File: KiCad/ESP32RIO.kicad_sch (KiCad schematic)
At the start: 44 parts, among them J1 Screw_Terminal_01x08, J2 Screw_Terminal_01x08, J3 Screw_Terminal_01x08, J4 Screw_Terminal_01x08, Q1 BC548, Q2 BC548, U1 PC817, U10 PC817, U11 PC817, U12 PC817, U13 PC817, U14 PC817, U15 LM7812_TO220, U16 ESP32-DEVKIT-V1, U17 XTR115U, U18 XTR115U, U19 PCF8574, U2 PC817, U20 ULN2803A, U21 TB67H451FNG, U22 SP3485CN, U3 PC817, U4 PC817, U5 PC817, U6 PC817, U7 PC817, U8 PC817, U9 PC817

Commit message: Versjon1
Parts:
- removed J1, J2, J3, J4: Screw_Terminal_01x08, TerminalBlock_Phoenix:TerminalBlock_Phoenix_MKDS-1,5-8-5.08_1x08_P5.08mm_Horizontal, symbol Connector:Screw_Terminal_01x08
- removed Q1, Q2: BC548, Package_TO_SOT_THT:TO-92_Inline, symbol Transistor_BJT:BC548
- removed U11, U12, U13, U14: PC817, Package_DIP:DIP-4_W7.62mm, symbol Isolator:PC817
- removed U15: LM7812_TO220, Package_TO_SOT_THT:TO-220-3_Vertical, symbol Regulator_Linear:LM7812_TO220
- removed U16: ESP32-DEVKIT-V1, doit-esp32-devkit-kicad:ESP32-DOIT-DEVKIT, symbol Devkit V1-1:ESP32-DEVKIT-V1
- removed U17, U18: XTR115U, Package_SO:SOIC-8_3.9x4.9mm_P1.27mm, symbol Interface_CurrentLoop:XTR115U
- removed U19: PCF8574, Package_DIP:DIP-18_W7.62mm, symbol Interface_Expansion:PCF8574
- removed U20: ULN2803A, Package_DIP:DIP-18_W7.62mm, symbol Transistor_Array:ULN2803A
- added C2, C3: 0.1uF, Capacitor_SMD:C_1206_3216Metric_Pad1.33x1.80mm_HandSolder, symbol RS485_Breakout-eagle-import:0.1UF-25V(+80/-20%)(0603)
- added C4: 47uF, Capacitor_THT:CP_Radial_D4.0mm_P2.00mm, symbol RS485_Breakout-eagle-import:0.1UF-25V(+80/-20%)(0603)
- added J1, J2: Screw_Terminal_01x12, TerminalBlock_Phoenix:TerminalBlock_Phoenix_MKDS-1,5-12_1x12_P5.00mm_Horizontal, symbol Connector:Screw_Terminal_01x12
- added R16, R17: R, Resistor_THT:R_Axial_DIN0204_L3.6mm_D1.6mm_P2.54mm_Vertical, symbol Device:R
- added U11: WeMos_S2_mini, wemos 2s mini:WEMOS_S2_mini, symbol Wemos s2 mini:WeMos_S2_mini
- added U12, U13, U14, U16: TLP222A, Package_DIP:DIP-4_W7.62mm, symbol Relay_SolidState:TLP222A
- added U15: L7805, Package_TO_SOT_SMD:TO-263-2, symbol Regulator_Linear:L7805
- C1: footprint RS485_Breakout:0603-CAP -> Capacitor_SMD:C_1206_3216Metric_Pad1.33x1.80mm_HandSolder
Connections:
- net +24V: now also J1.3 (Pin_3), U15.1 (IN)
- net GND: now also C1.2, U1.3, U10.3, U2.3, U21.1 (GND), U21.7 (RS), U21.9 (PAD), U22.5 (GND), U3.3, U4.3, U5.3, U6.3, U7.3, U8.3, U9.3, C2.1, C3.2, C4.1, J1.9 (Pin_9), R16.1, R17.1, U11.10 (GND), U11.26 (GND), U12.2, U13.2, U14.2, U15.2 (GND), U16.2
- net RTS: now also U11.23 (GPIO13)
- net RX-I: now also U11.7 (GPIO12)
- net TX-O: now also U11.24 (GPIO14)
- net at R4.2: now also J2.4 (Pin_4)
- net at R6.2: now also J2.6 (Pin_6)
- net at R15.1, U22.6 (A): now also J1.1 (Pin_1)
- net at R15.2, U22.7 (B): now also J1.2 (Pin_2)
- net at U10.4: now also U11.12 (GPIO18)
- net at R7.2: now also J2.7 (Pin_7)
- net at U6.4: now also U11.14 (GPIO35)
- net at U3.4: now also U11.31 (GPIO38)
- net at R13.1: now also U14.1
- net at C1.1: now also U21.4 (VREF), U22.8 (VCC), C3.1, U11.8 (3V3)
- net at R2.2: now also J2.2 (Pin_2)
- net at R13.2: now also U11.22 (GPIO10)
- net at R14.1: now also U16.1
- net at R14.2: now also U11.6 (GPIO11)
- net at R9.2: now also J2.9 (Pin_9)
- net at U7.4: now also U11.29 (GPIO34)
- net at U21.5 (VM): now also C2.2, C4.2, J1.10 (Pin_10)
- net at U21.8 (OUT2): now also J1.12 (Pin_12)
- net at U21.6 (OUT1): now also J1.11 (Pin_11)
- net at R12.1: now also U13.1
- net at R8.2: now also J2.8 (Pin_8)
- net at U4.4: now also U11.15 (GPIO37)
- net at R12.2: now also U11.5 (GPIO9)
- net at U1.4: now also U11.32 (GPIO40)
- net at R10.2: now also J2.10 (Pin_10)
- net at R11.1: now also U12.1
- net at R5.2: now also J2.5 (Pin_5)
- net at U2.4: now also U11.16 (GPIO39)
- net at U21.2 (IN2): now also U11.18 (GPIO2)
- net at U21.3 (IN1): now also U11.2 (GPIO3)
- net at R1.2: now also J2.1 (Pin_1)
- net at U9.4: now also U11.28 (GPIO21)
- net at R3.2: now also J2.3 (Pin_3)
- net at U8.4: now also U11.13 (GPIO33)
- net at R11.2: now also U11.21 (GPIO8)
- net at U5.4: now also U11.30 (GPIO36)
- new net: J2.12 (Pin_12), R16.2, U11.27 (GPIO17)
- new net: J2.11 (Pin_11), R17.2, U11.11 (GPIO16)
- new net: U11.9 (VBUS), U15.3 (OUT)
- new net: J1.4 (Pin_4), U12.3, U13.3, U14.3, U16.3
- new net: J1.5 (Pin_5), U16.4
- new net: J1.6 (Pin_6), U14.4
- new net: J1.7 (Pin_7), U13.4
- new net: J1.8 (Pin_8), U12.4
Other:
- note removed: "AI1"
- note removed: "AI2"
- note removed: "D2 må ha egen pullup motstand"
- note removed: "DAC"
- note removed: "Må bruke AM 422-1"
- moved on the sheet: C1, U21

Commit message: v1 sendt til produksjon
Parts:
- R11: value R -> 120R
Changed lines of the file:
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@@
       (effects (font (size 1.27 1.27)))
     )
-    (property "Value" "R" (at 220.98 55.4736 90)
+    (property "Value" "120R" (at 220.98 55.4736 90)
       (effects (font (size 1.27 1.27)))
     )

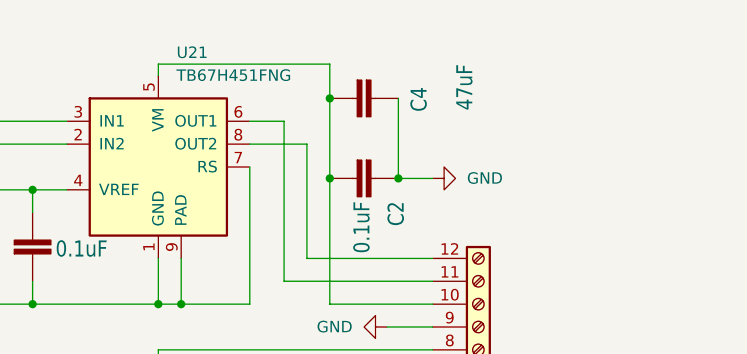
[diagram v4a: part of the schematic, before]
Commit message: fix kondensator og regulator
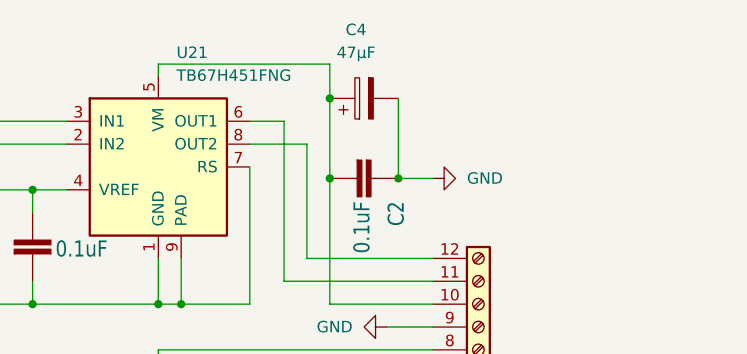
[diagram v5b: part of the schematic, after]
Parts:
- removed C4: 47uF, Capacitor_THT:CP_Radial_D4.0mm_P2.00mm, symbol RS485_Breakout-eagle-import:0.1UF-25V(+80/-20%)(0603)
- added C4: 47µF, Capacitor_THT:CP_Radial_D5.0mm_P2.50mm, symbol Device:C_Polarized
- U15: footprint Package_TO_SOT_SMD:TO-263-2 -> Package_TO_SOT_SMD:TO-252-2
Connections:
- net GND: now also C4.2
- net at C2.2, J1.10 (Pin_10), U21.5 (VM): now also C4.1
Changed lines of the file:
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@@
   (junction (at 229.87 163.83) (diameter 0) (color 0 0 0 0)
   )
+  (junction (at 64.77 72.39) (diameter 0) (color 0 0 0 0)
+  )
+  (junction (at 275.59 91.44) (diameter 0) (color 0 0 0 0)
+  )
+  (junction (at 85.09 132.08) (diameter 0) (color 0 0 0 0)
+  )
+  (junction (at 64.77 99.06) (diameter 0) (color 0 0 0 0)
+  )
+  (junction (at 85.09 116.84) (diameter 0) (color 0 0 0 0)
+  )
+  (junction (at 85.09 72.39) (diameter 0) (color 0 0 0 0)
+  )
+  (junction (at 64.77 107.95) (diameter 0) (color 0 0 0 0)
+  )
+  (junction (at 85.09 125.73) (diameter 0) (color 0 0 0 0)
+  )
+  (junction (at 255.27 95.25) (diameter 0) (color 0 0 0 0)
+  )
+  (junction (at 255.27 63.5) (diameter 0) (color 0 0 0 0)
+  )
+  (junction (at 45.72 90.17) (diameter 0) (color 0 0 0 0)
+  )
+  (junction (at 64.77 54.61) (diameter 0) (color 0 0 0 0)
+  )
+  (junction (at 85.09 90.17) (diameter 0) (color 0 0 0 0)
+  )
+  (junction (at 151.13 132.08) (diameter 0) (color 0 0 0 0)
+  )
+  (junction (at 247.65 40.64) (diameter 0) (color 0 0 0 0)
+  )
+  (junction (at 125.73 132.08) (diameter 0) (color 0 0 0 0)
+  )
   (junction (at 264.16 17.78) (diameter 0) (color 0 0 0 0)
   )
-  (junction (at 64.77 72.39) (diameter 0) (color 0 0 0 0)
-  )
-  (junction (at 275.59 91.44) (diameter 0) (color 0 0 0 0)
-  )
-  (junction (at 85.09 132.08) (diameter 0) (color 0 0 0 0)
-  )
-  (junction (at 64.77 99.06) (diameter 0) (color 0 0 0 0)
-  )
-  (junction (at 85.09 116.84) (diameter 0) (color 0 0 0 0)
-  )
-  (junction (at 85.09 72.39) (diameter 0) (color 0 0 0 0)
-  )
-  (junction (at 64.77 107.95) (diameter 0) (color 0 0 0 0)
-  )
-  (junction (at 85.09 125.73) (diameter 0) (color 0 0 0 0)
-  )
-  (junction (at 255.27 95.25) (diameter 0) (color 0 0 0 0)
-  )
-  (junction (at 255.27 63.5) (diameter 0) (color 0 0 0 0)
-  )
-  (junction (at 45.72 90.17) (diameter 0) (color 0 0 0 0)
-  )
-  (junction (at 64.77 54.61) (diameter 0) (color 0 0 0 0)
-  )
-  (junction (at 85.09 90.17) (diameter 0) (color 0 0 0 0)
-  )
-  (junction (at 151.13 132.08) (diameter 0) (color 0 0 0 0)
-  )
-  (junction (at 247.65 40.64) (diameter 0) (color 0 0 0 0)
-  )
-  (junction (at 125.73 132.08) (diameter 0) (color 0 0 0 0)
-  )
   (junction (at 85.09 81.28) (diameter 0) (color 0 0 0 0)
   )
@@
     (stroke (width 0) (type default))
   )
+  (wire (pts (xy 264.16 17.78) (xy 264.16 26.67))
+    (stroke (width 0) (type default))
+  )
   (wire (pts (xy 111.76 68.58) (xy 111.76 137.16))
     (stroke (width 0) (type default))
@@
     (stroke (width 0) (type default))
   )
-  (wire (pts (xy 264.16 17.78) (xy 264.16 26.67))
+  (wire (pts (xy 264.16 13.97) (xy 264.16 17.78))
     (stroke (width 0) (type default))
   )
@@
   )
   (wire (pts (xy 227.33 95.25) (xy 229.87 95.25))
-    (stroke (width 0) (type default))
-  )
-  (wire (pts (xy 264.16 13.97) (xy 264.16 17.78))
     (stroke (width 0) (type default))
   )
@@
     )
   )
-  (symbol (lib_id "RS485_Breakout-eagle-import:0.1UF-25V(+80{slash}-20%)(0603)") (at 266.7 17.78 270) (unit 1)
-    (in_bom yes) (on_board yes) (dnp no)
-    (property "Reference" "C4" (at 273.05 16.51 0)
-      (effects (font (size 1.778 1.5113)) (justify left bottom))
-    )
-    (property "Value" "47uF" (at 278.13 13.97 0)
-      (effects (font (size 1.778 1.5113)) (justify left bottom))
-    )
-    (property "Footprint" "Capacitor_THT:CP_Radial_D4.0mm_P2.00mm" (at 266.7 17.78 0)
-      (effects (font (size 1.27 1.27)) hide)
-    )
-    (property "Datasheet" "" (at 266.7 17.78 0)
-      (effects (font (size 1.27 1.27)) hide)
-    )
-    (pin "1")
-    (pin "2")
-    (instances
-      (project "ESP32RIO"
-        (path "/b73dfc04-f27f-4656-9661-136d79422d6f"
-          (reference "C4") (unit 1)
-        )
-      )
-    )
-  )
   (symbol (lib_id "Device:R") (at 220.98 104.14 270) (unit 1)
     (in_bom yes) (on_board yes) (dnp no)
@@
         (path "/b73dfc04-f27f-4656-9661-136d79422d6f"
           (reference "R12") (unit 1)
+        )
+      )
+    )
+  )
+  (symbol (lib_id "Device:C_Polarized") (at 267.97 17.78 90) (unit 1)
+    (in_bom yes) (on_board yes) (dnp no) (fields_autoplaced)
+    (property "Reference" "C4" (at 267.081 10.16 90)
+      (effects (font (size 1.27 1.27)))
+    )
+    (property "Value" "47µF" (at 267.081 12.7 90)
+      (effects (font (size 1.27 1.27)))
+    )
+    (property "Footprint" "Capacitor_THT:CP_Radial_D5.0mm_P2.50mm" (at 271.78 16.8148 0)
+      (effects (font (size 1.27 1.27)) hide)
+    )
+    (property "Datasheet" "~" (at 267.97 17.78 0)
+      (effects (font (size 1.27 1.27)) hide)
+    )
+    (pin "1")
+    (pin "2")
+    (instances
+      (project "ESP32RIO"
+        (path "/b73dfc04-f27f-4656-9661-136d79422d6f"
+          (reference "C4") (unit 1)
         )
       )
@@
       (effects (font (size 1.27 1.27)))
     )
-    (property "Footprint" "Package_TO_SOT_SMD:TO-263-2" (at 150.495 114.3 0)
+    (property "Footprint" "Package_TO_SOT_SMD:TO-252-2" (at 150.495 114.3 0)
       (effects (font (size 1.27 1.27) italic) (justify left) hide)
     )

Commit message: v1-finish
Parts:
- added D1, D2: D_TVS, symbol Device:D_TVS
- added TH1, TH2: Thermistor_PTC, symbol Device:Thermistor_PTC
- added U17: ~, Package_SO:SOP-4_3.8x4.1mm_P2.54mm, symbol Fred-Olav:EL3H7-G
- added U18: PC817, Package_DIP:DIP-4_W7.62mm, symbol Isolator:PC817
- C1, C2, C3: symbol RS485_Breakout-eagle-import:0.1UF-25V(+80/-20%)(0603) -> RS485_Breakout-eagle-import:0.1UF-25V(+80/-20%)(0603)
- R16, R17: value R -> 250R
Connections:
- net GND: now also D1.1 (A1), D2.2 (A2)
- net at R16.2, U11.27 (GPIO17): now also D2.1 (A1), TH2.2; no longer J2.12 (Pin_12)
- net at R17.2, U11.11 (GPIO16): now also D1.2 (A2), TH1.2; no longer J2.11 (Pin_11)
- new net: J2.11 (Pin_11), TH1.1
- new net: J2.12 (Pin_12), TH2.1
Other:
- moved on the sheet: R16, R17
